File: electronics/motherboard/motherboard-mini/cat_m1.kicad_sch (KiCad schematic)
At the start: 38 parts, among them J11 CONUFL001-SMD-T, J12 SIM8060-6-0-14-00-A, Q4 BC847, Q5 BC847, SW3 CAT_M1_RST, U11 TPS22967DSGR, U12 SARA-R410M-02B, U13 TXB0104PW

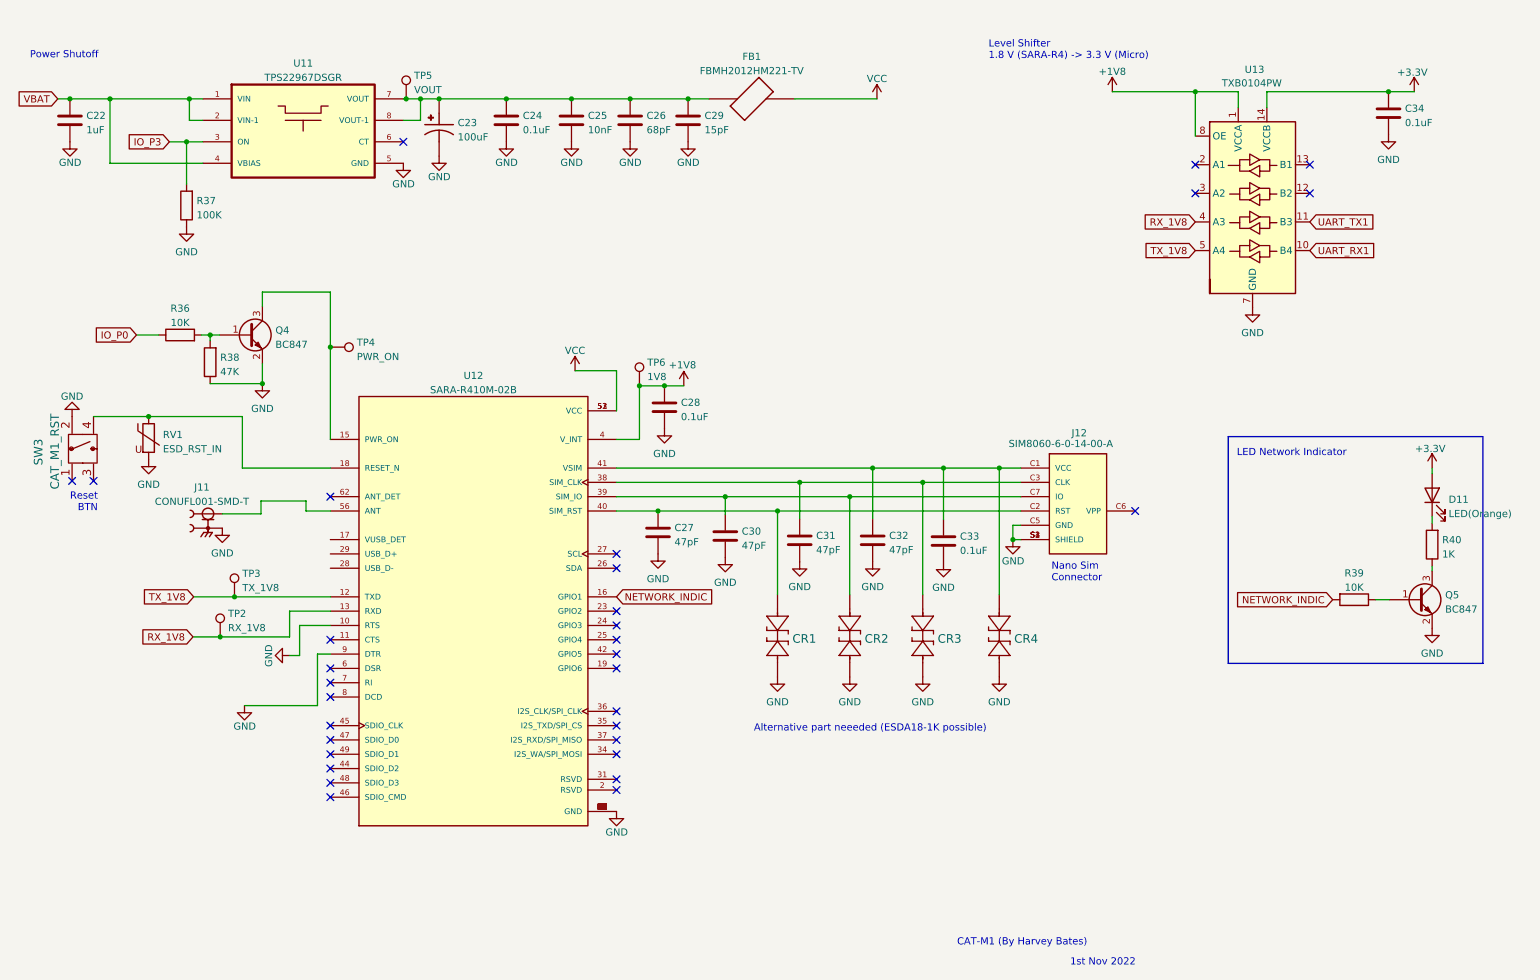
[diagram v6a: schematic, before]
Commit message: refactored schemematics and added pdf previews for readme
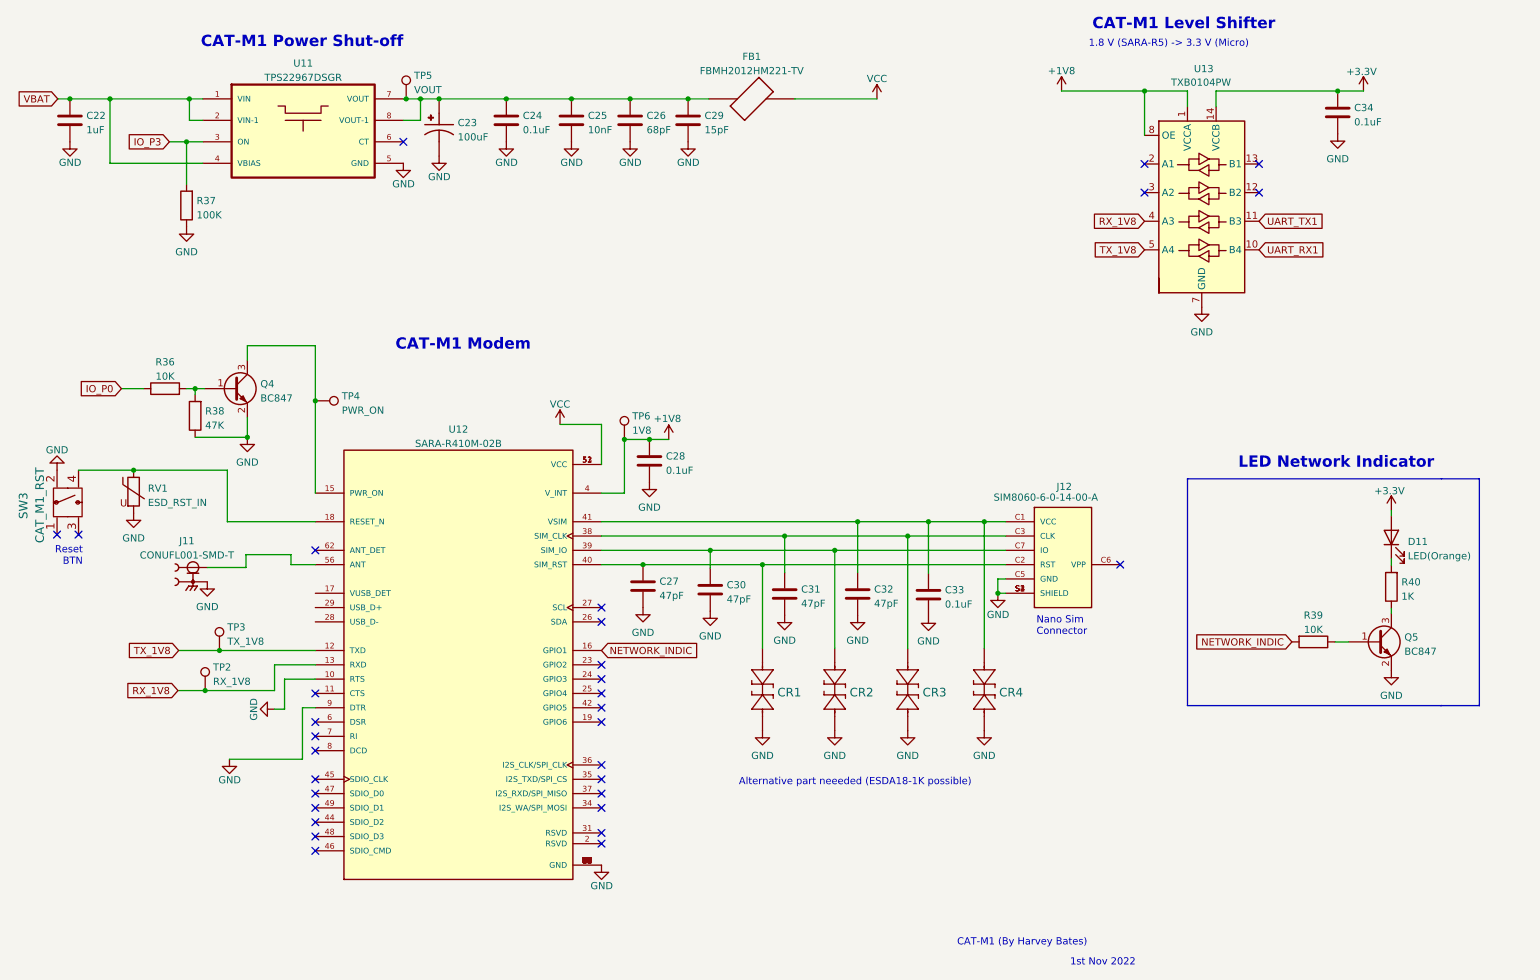
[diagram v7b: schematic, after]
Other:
- note added: "1.8 V (SARA-R5) -> 3.3 V (Micro)"
- note added: "CAT-M1 Level Shifter"
- note added: "CAT-M1 Modem"
- note added: "CAT-M1 Power Shut-off"
- note removed: "Level Shifter 1.8 V (SARA-R4) -> 3.3 V (Micro)"
- note removed: "Power Shutoff"
- company: (none) -> NSW Department of Primary Industries
- title: (none) -> Enviro-node
- moved on the sheet: C27, C28, C30, C31, C32, C33, C34, CR1, CR2, CR3, CR4, D11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
